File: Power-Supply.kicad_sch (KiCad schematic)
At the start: 18 parts, among them J1 CON_USB_GCT_USB4105_REVA, J2 DC, U11 MIC5212-SJYM, U6 LDK130-12_SOT23_SOT353

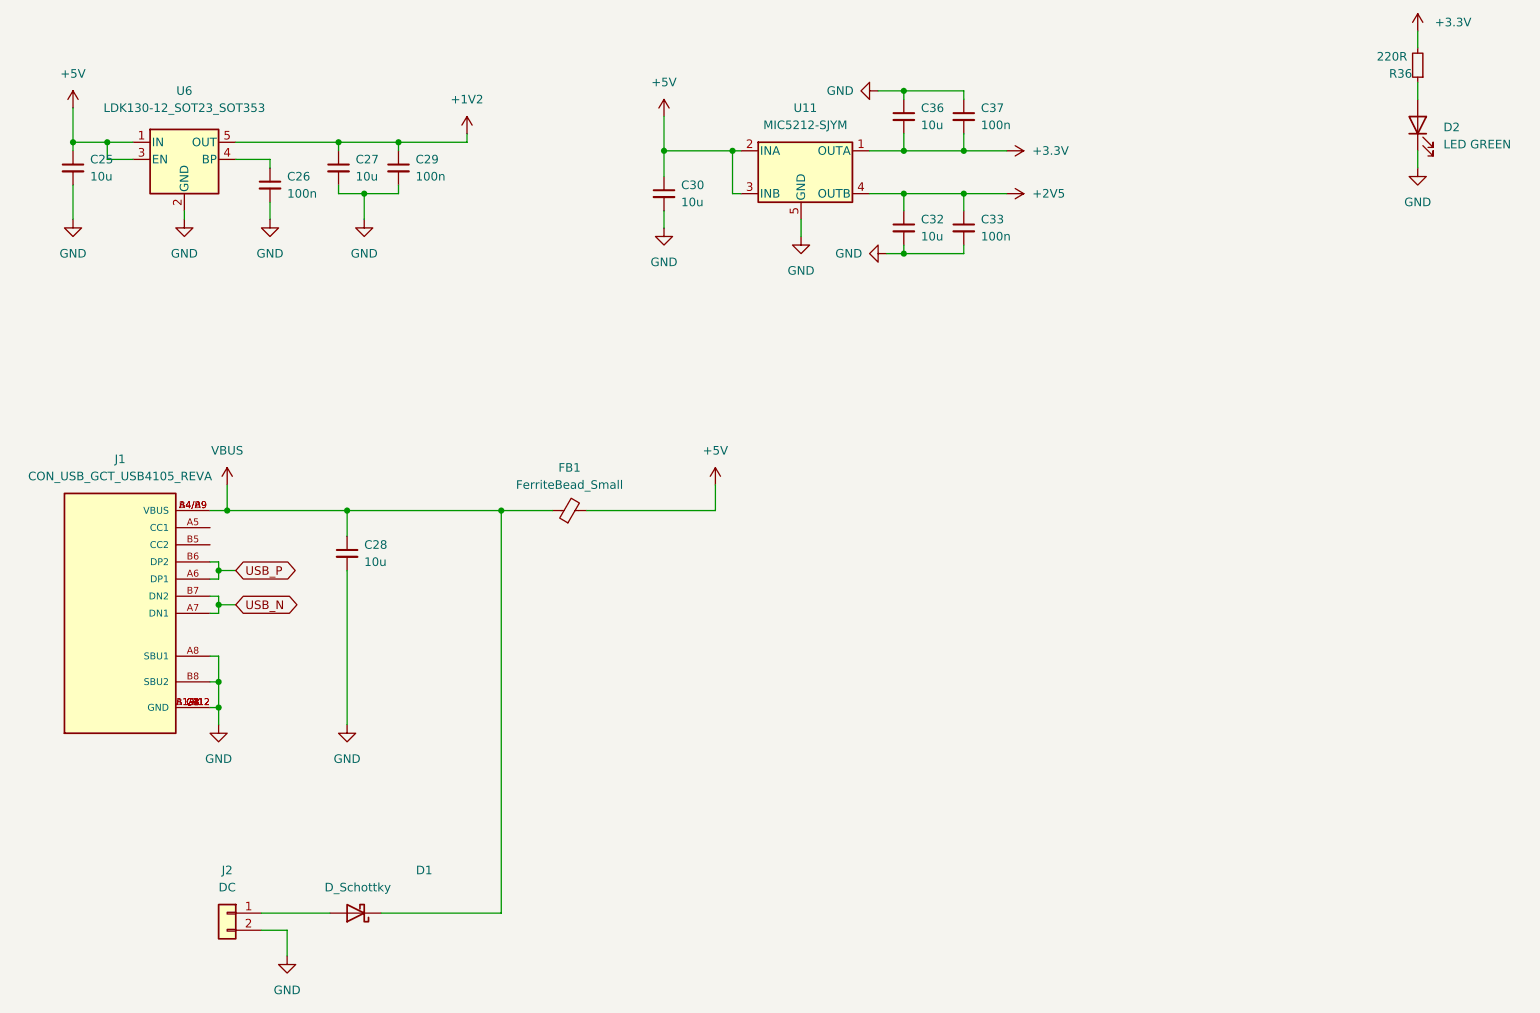
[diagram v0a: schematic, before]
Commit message: Update the description
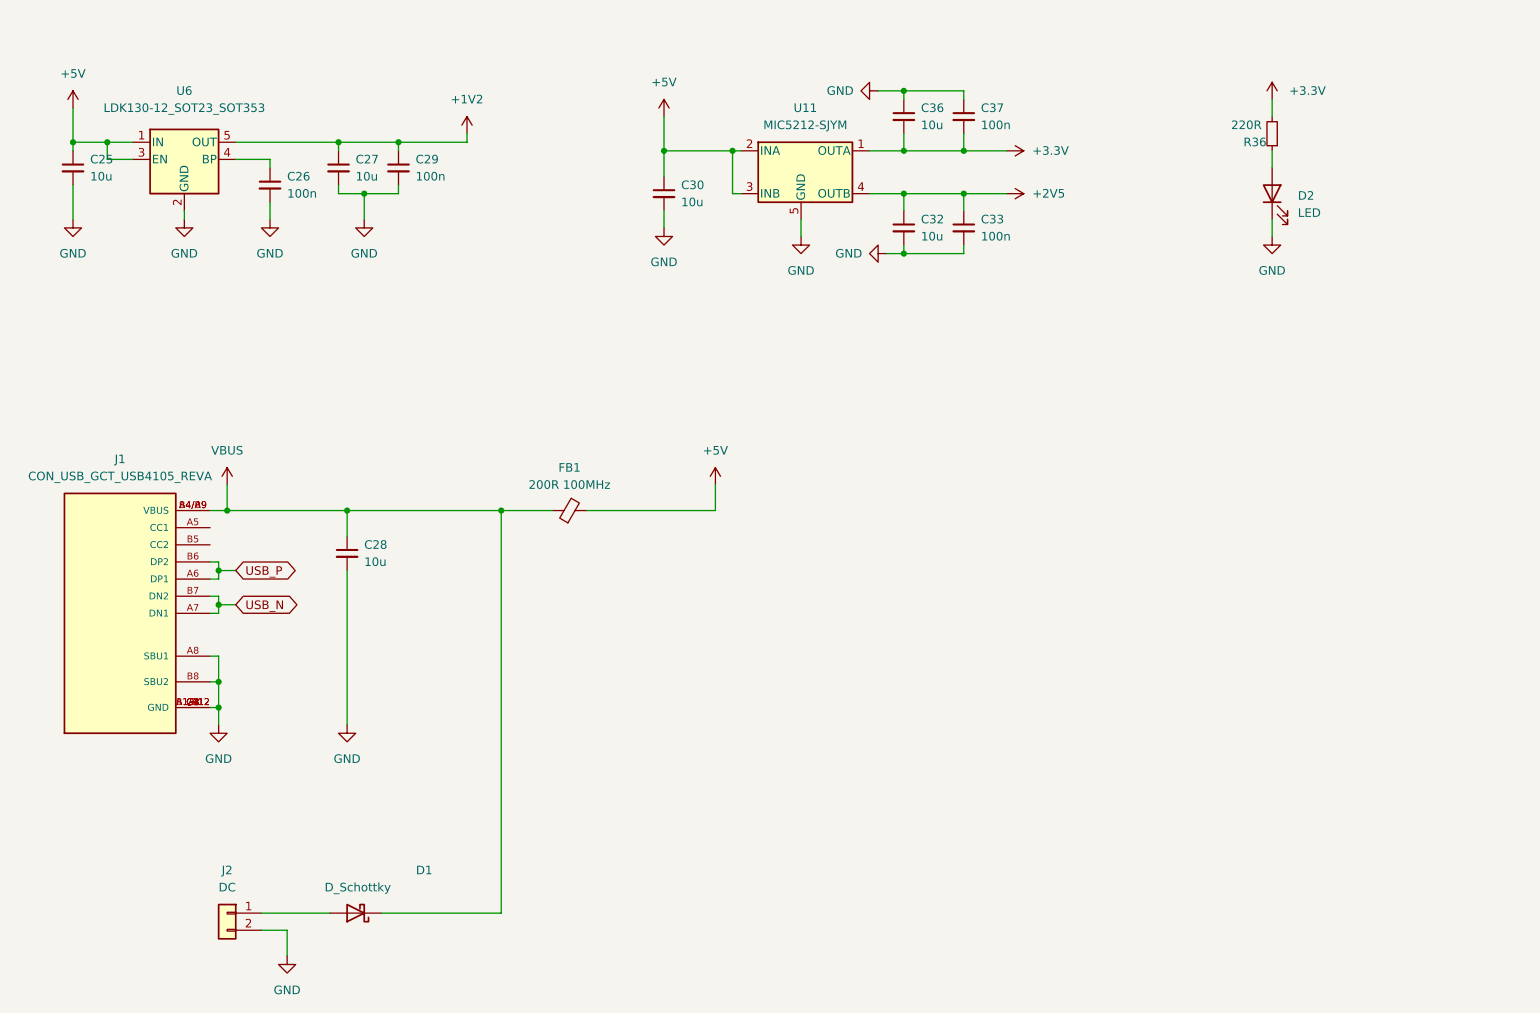
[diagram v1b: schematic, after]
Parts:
- D2: value LED GREEN -> LED
- FB1: value FerriteBead_Small -> 200R 100MHz
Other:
- moved on the sheet: D2, R36
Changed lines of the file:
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@@
     (stroke (width 0) (type default) (color 0 0 0 0))
   )
-  (wire (pts (xy 237.49 46.99) (xy 237.49 49.53))
+  (wire (pts (xy 215.9 57.15) (xy 215.9 59.69))
     (stroke (width 0) (type default) (color 0 0 0 0))
   )
@@
     (stroke (width 0) (type default) (color 0 0 0 0))
   )
-  (wire (pts (xy 237.49 36.83) (xy 237.49 39.37))
+  (wire (pts (xy 215.9 46.99) (xy 215.9 49.53))
     (stroke (width 0) (type default) (color 0 0 0 0))
   )
@@
     (stroke (width 0) (type default) (color 0 0 0 0))
   )
-  (wire (pts (xy 237.49 29.21) (xy 237.49 31.75))
+  (wire (pts (xy 215.9 39.37) (xy 215.9 41.91))
     (stroke (width 0) (type default) (color 0 0 0 0))
   )
@@
     (in_bom yes) (on_board yes) (fields_autoplaced)
     (property "Reference" "FB1" (id 0) (at 111.7219 93.98 90))
-    (property "Value" "FerriteBead_Small" (id 1) (at 111.7219 96.52 90))
+    (property "Value" "200R 100MHz" (id 1) (at 111.7219 96.52 90))
     (property "Footprint" "Capacitor_SMD:C_1206_3216Metric" (id 2) (at 111.76 102.108 90)
       (effects (font (size 1.27 1.27)) hide)
@@
     (pin "2")
   )
-  (symbol (lib_id "Device:LED") (at 237.49 43.18 90) (unit 1)
-    (in_bom yes) (on_board yes) (fields_autoplaced)
-    (property "Reference" "D2" (id 0) (at 241.3 43.4974 90)
+  (symbol (lib_id "Device:LED") (at 215.9 53.34 90) (unit 1)
+    (in_bom yes) (on_board yes) (fields_autoplaced)
+    (property "Reference" "D2" (id 0) (at 219.71 53.6574 90)
       (effects (font (size 1.27 1.27)) (justify right))
     )
-    (property "Value" "LED GREEN" (id 1) (at 241.3 46.0374 90)
+    (property "Value" "LED" (id 1) (at 219.71 56.1974 90)
       (effects (font (size 1.27 1.27)) (justify right))
     )
-    (property "Footprint" "LED_SMD:LED_0603_1608Metric" (id 2) (at 237.49 43.18 0)
-      (effects (font (size 1.27 1.27)) hide)
-    )
-    (property "Datasheet" "~" (id 3) (at 237.49 43.18 0)
+    (property "Footprint" "LED_SMD:LED_0603_1608Metric" (id 2) (at 215.9 53.34 0)
+      (effects (font (size 1.27 1.27)) hide)
+    )
+    (property "Datasheet" "~" (id 3) (at 215.9 53.34 0)
       (effects (font (size 1.27 1.27)) hide)
     )
@@
     (pin "2")
   )
-  (symbol (lib_id "power:+3.3V") (at 237.49 29.21 0) (unit 1)
-    (in_bom yes) (on_board yes) (fields_autoplaced)
-    (property "Reference" "#PWR014" (id 0) (at 237.49 33.02 0)
-      (effects (font (size 1.27 1.27)) hide)
-    )
-    (property "Value" "+3.3V" (id 1) (at 240.03 27.9399 0)
-      (effects (font (size 1.27 1.27)) (justify left))
-    )
-    (property "Footprint" "" (id 2) (at 237.49 29.21 0)
-      (effects (font (size 1.27 1.27)) hide)
-    )
-    (property "Datasheet" "" (id 3) (at 237.49 29.21 0)
+  (symbol (lib_id "power:+3.3V") (at 215.9 39.37 0) (unit 1)
+    (in_bom yes) (on_board yes) (fields_autoplaced)
+    (property "Reference" "#PWR014" (id 0) (at 215.9 43.18 0)
+      (effects (font (size 1.27 1.27)) hide)
+    )
+    (property "Value" "+3.3V" (id 1) (at 218.44 38.0999 0)
+      (effects (font (size 1.27 1.27)) (justify left))
+    )
+    (property "Footprint" "" (id 2) (at 215.9 39.37 0)
+      (effects (font (size 1.27 1.27)) hide)
+    )
+    (property "Datasheet" "" (id 3) (at 215.9 39.37 0)
       (effects (font (size 1.27 1.27)) hide)
     )
@@
     (pin "G4")
   )
-  (symbol (lib_id "power:GND") (at 237.49 49.53 0) (unit 1)
-    (in_bom yes) (on_board yes) (fields_autoplaced)
-    (property "Reference" "#PWR015" (id 0) (at 237.49 55.88 0)
-      (effects (font (size 1.27 1.27)) hide)
-    )
-    (property "Value" "GND" (id 1) (at 237.49 54.61 0))
-    (property "Footprint" "" (id 2) (at 237.49 49.53 0)
-      (effects (font (size 1.27 1.27)) hide)
-    )
-    (property "Datasheet" "" (id 3) (at 237.49 49.53 0)
+  (symbol (lib_id "power:GND") (at 215.9 59.69 0) (unit 1)
+    (in_bom yes) (on_board yes) (fields_autoplaced)
+    (property "Reference" "#PWR015" (id 0) (at 215.9 66.04 0)
+      (effects (font (size 1.27 1.27)) hide)
+    )
+    (property "Value" "GND" (id 1) (at 215.9 64.77 0))
+    (property "Footprint" "" (id 2) (at 215.9 59.69 0)
+      (effects (font (size 1.27 1.27)) hide)
+    )
+    (property "Datasheet" "" (id 3) (at 215.9 59.69 0)
       (effects (font (size 1.27 1.27)) hide)
     )
@@
     (pin "1")
   )
-  (symbol (lib_id "Device:R_Small") (at 237.49 34.29 180) (unit 1)
+  (symbol (lib_id "Device:R_Small") (at 215.9 44.45 180) (unit 1)
     (in_bom yes) (on_board yes)
-    (property "Reference" "R36" (id 0) (at 234.95 35.56 0))
-    (property "Value" "220R" (id 1) (at 233.68 33.02 0))
-    (property "Footprint" "Resistor_SMD:R_0603_1608Metric" (id 2) (at 237.49 34.29 0)
-      (effects (font (size 1.27 1.27)) hide)
-    )
-    (property "Datasheet" "~" (id 3) (at 237.49 34.29 0)
-      (effects (font (size 1.27 1.27)) hide)
-    )
+    (property "Reference" "R36" (id 0) (at 213.36 45.72 0))
+    (property "Value" "220R" (id 1) (at 212.09 43.18 0))
+    (property "Footprint" "Resistor_SMD:R_0603_1608Metric" (id 2) (at 215.9 44.45 0)
+      (effects (font (size 1.27 1.27)) hide)
+    )
+    (property "Datasheet" "~" (id 3) (at 215.9 44.45 0)
+      (effects (font (size 1.27 1.27)) hide)
+    )
